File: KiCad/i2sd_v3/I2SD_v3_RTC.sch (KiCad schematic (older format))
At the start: 6 parts, among them U4 DS3231N

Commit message: i2sd_v3 : 2011 Nov 22 added INT/SQW 1Hz to PD2 port of ATMega via solder bridge, near Screw/RST Switch
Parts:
- added B20: I/O, I/O, symbol I/O
- added R9: 10k, symbol R
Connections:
- net labels added: 1Hz, B_03
- wire segments 35 -> 38
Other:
- note added: "Solder Bridge betn\nB2 & B20 to get 1Hz"
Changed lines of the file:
@@
-EESchema Schematic File Version 2  date 11/18/2011 6:47:08 PM
+EESchema Schematic File Version 2  date 11/22/2011 6:28:42 PM
 LIBS:i2sd_v3
 LIBS:power
@@
 Sheet 2 2
 Title "Buckler, i2sd, v3, with RTC, with HW addressing"
-Date "18 nov 2011"
+Date "22 nov 2011"
 Rev "3"
 Comp "WyoLum"
@@
 Comment4 ""
 $EndDescr
+Text Notes 7950 2225 2    50   ~ 0
+Solder Bridge betn\nB2 & B20 to get 1Hz
+Text HLabel 7825 2450 2    50   Input ~ 0
+B_03
+Text Label 7550 2450 0    50   ~ 0
+1Hz
+Wire Wire Line
+	7400 2450 7825 2450
+Connection ~ 6650 1675
+Wire Wire Line
+	6650 1850 6650 1675
+Wire Wire Line
+	7250 3750 7050 3750
+Wire Wire Line
+	7050 3750 7050 1675
+Wire Wire Line
+	7050 1675 4375 1675
+Wire Wire Line
+	6450 2600 6675 2600
+Wire Wire Line
+	7250 4000 4500 4000
+Wire Wire Line
+	4500 4000 4500 2850
+Wire Wire Line
+	4500 2850 4650 2850
+Connection ~ 3950 3100
+Wire Wire Line
+	3950 3100 4175 3100
+Wire Wire Line
+	4175 3100 4175 2975
+Wire Wire Line
+	3950 2550 3950 1900
+Wire Wire Line
+	3950 1900 5300 1900
+Connection ~ 6575 3150
+Wire Wire Line
+	6575 3150 6450 3150
+Connection ~ 6575 2950
+Wire Wire Line
+	6450 2950 6575 2950
+Connection ~ 5850 3750
+Wire Wire Line
+	5850 3750 5850 3650
+Wire Wire Line
+	5750 3750 5750 3650
+Wire Wire Line
+	6575 2850 6575 3750
+Wire Wire Line
+	6575 2850 6450 2850
+Wire Wire Line
+	4650 2600 4375 2600
+Connection ~ 5750 3750
+Wire Wire Line
+	5950 3750 5950 3650
+Connection ~ 5950 3750
+Wire Wire Line
+	6575 3050 6450 3050
+Connection ~ 6575 3050
+Wire Wire Line
+	6450 3250 6575 3250
+Connection ~ 6575 3250
+Wire Wire Line
+	4650 2450 4375 2450
+Wire Wire Line
+	3950 3000 3950 3750
+Wire Wire Line
+	3950 3750 6575 3750
+Connection ~ 4375 3750
+Wire Wire Line
+	4175 2575 4175 2425
+Wire Wire Line
+	4175 2425 3950 2425
+Connection ~ 3950 2425
+Wire Wire Line
+	4375 2450 4375 1675
+Wire Wire Line
+	4650 3000 4550 3000
+Wire Wire Line
+	4550 3000 4550 3875
+Wire Wire Line
+	4550 3875 7250 3875
+Wire Wire Line
+	6675 2450 6450 2450
+Wire Wire Line
+	6675 2750 6450 2750
+Wire Wire Line
+	4375 2600 4375 4125
+Wire Wire Line
+	4375 4125 7250 4125
+Wire Wire Line
+	5300 1850 5300 2000
+Connection ~ 5300 1900
+Wire Wire Line
+	6650 2350 6650 2450
+Connection ~ 6650 2450
+$Comp
+L I/O B20
+U 1 1 4ECB8D5B
+P 7250 2450
+F 0 "B20" H 7330 2450 40  0000 L CNN
+F 1 "I/O" H 7250 2505 30  0001 C CNN
+F 2 "I/O" H 7250 2450 60  0001 C CNN
+	1    7250 2450
+	-1   0    0    1
+$EndComp
+$Comp
+L R R9
+U 1 1 4ECB8D22
+P 6650 2100
+F 0 "R9" V 6730 2100 50  0000 C CNN
+F 1 "10k" V 6650 2100 50  0000 C CNN
+	1    6650 2100
+	1    0    0    -1
+$EndComp
 $Comp
 L +BATT #PWR09
@@
 	1    0    0    -1
 $EndComp
-Connection ~ 5300 1900
-Wire Wire Line
-	5300 1850 5300 2000
-Wire Wire Line
-	7250 4125 4375 4125
-Wire Wire Line
-	4375 4125 4375 2600
-Wire Wire Line
-	6675 2750 6450 2750
-Wire Wire Line
-	6675 2450 6450 2450
-Wire Wire Line
-	7250 3875 4550 3875
-Wire Wire Line
-	4550 3875 4550 3000
-Wire Wire Line
-	4550 3000 4650 3000
-Wire Wire Line
-	4375 2450 4375 1675
-Connection ~ 3950 2425
-Wire Wire Line
-	3950 2425 4175 2425
-Wire Wire Line
-	4175 2425 4175 2575
-Connection ~ 4375 3750
-Wire Wire Line
-	3950 3750 6575 3750
-Wire Wire Line
-	3950 3750 3950 3000
-Wire Wire Line
-	4375 2450 4650 2450
-Connection ~ 6575 3250
-Wire Wire Line
-	6450 3250 6575 3250
-Connection ~ 6575 3050
-Wire Wire Line
-	6575 3050 6450 3050
-Connection ~ 5950 3750
-Wire Wire Line
-	5950 3750 5950 3650
-Connection ~ 5750 3750
-Wire Wire Line
-	4375 2600 4650 2600
-Wire Wire Line
-	6450 2850 6575 2850
-Wire Wire Line
-	6575 2850 6575 3750
-Wire Wire Line
-	5750 3750 5750 3650
-Wire Wire Line
-	5850 3750 5850 3650
-Connection ~ 5850 3750
-Wire Wire Line
-	6450 2950 6575 2950
-Connection ~ 6575 2950
-Wire Wire Line
-	6575 3150 6450 3150
-Connection ~ 6575 3150
-Wire Wire Line
-	5300 1900 3950 1900
-Wire Wire Line
-	3950 1900 3950 2550
-Wire Wire Line
-	4175 2975 4175 3100
-Wire Wire Line
-	4175 3100 3950 3100
-Connection ~ 3950 3100
-Wire Wire Line
-	4650 2850 4500 2850
-Wire Wire Line
-	4500 2850 4500 4000
-Wire Wire Line
-	4500 4000 7250 4000
-Wire Wire Line
-	6450 2600 6675 2600
-Wire Wire Line
-	4375 1675 7050 1675
-Wire Wire Line
-	7050 1675 7050 3750
-Wire Wire Line
-	7050 3750 7250 3750
 Text HLabel 7250 4125 2    60   Input ~ 0
 GND

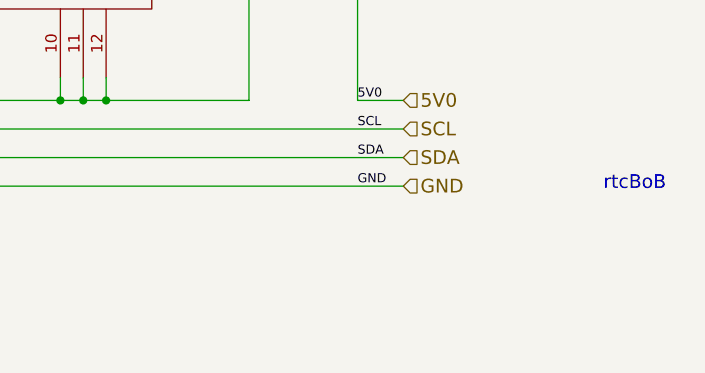
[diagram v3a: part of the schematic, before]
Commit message: i2sd_v3 : Silk screen changes, Box design, connected CD tracks
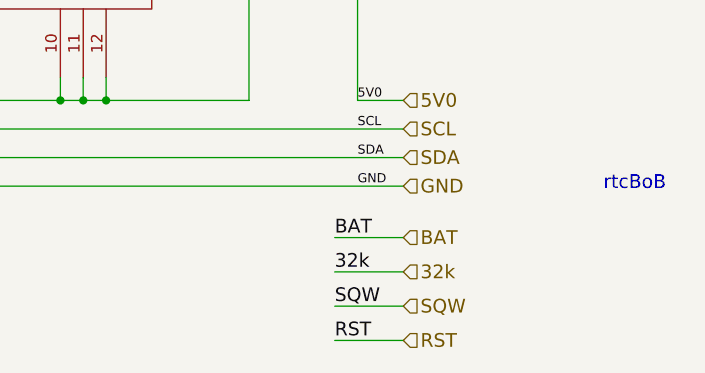
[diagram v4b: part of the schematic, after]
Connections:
- wire segments 38 -> 42
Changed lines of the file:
@@
-EESchema Schematic File Version 2  date 11/22/2011 6:28:42 PM
+EESchema Schematic File Version 2  date 1/12/2012 5:17:19 PM
 LIBS:i2sd_v3
 LIBS:power
@@
 Sheet 2 2
 Title "Buckler, i2sd, v3, with RTC, with HW addressing"
-Date "22 nov 2011"
+Date "12 jan 2012"
 Rev "3"
 Comp "WyoLum"
@@
 Comment4 ""
 $EndDescr
-Text Notes 7950 2225 2    50   ~ 0
-Solder Bridge betn\nB2 & B20 to get 1Hz
-Text HLabel 7825 2450 2    50   Input ~ 0
-B_03
-Text Label 7550 2450 0    50   ~ 0
-1Hz
+Text Label 6950 4800 0    60   ~ 0
+RST
+Text Label 6950 4650 0    60   ~ 0
+SQW
+Text Label 6950 4500 0    60   ~ 0
+32k
+Text Label 6950 4350 0    60   ~ 0
+BAT
+Wire Wire Line
+	7250 4800 6950 4800
+Wire Wire Line
+	7250 4500 6950 4500
 Wire Wire Line
 	7400 2450 7825 2450
@@
 	6650 2350 6650 2450
 Connection ~ 6650 2450
+Wire Wire Line
+	7250 4350 6950 4350
+Wire Wire Line
+	7250 4650 6950 4650
+Text HLabel 7250 4800 2    60   Input ~ 0
+RST
+Text HLabel 7250 4650 2    60   Input ~ 0
+SQW
+Text HLabel 7250 4500 2    60   Input ~ 0
+32k
+Text HLabel 7250 4350 2    60   Input ~ 0
+BAT
+Text Notes 7950 2225 2    50   ~ 0
+Solder Bridge betn\nB2 & B20 to get 1Hz
+Text HLabel 7825 2450 2    50   Input ~ 0
+B_03
+Text Label 7550 2450 0    50   ~ 0
+1Hz
 $Comp
 L I/O B20

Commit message: i2sd_v3 some minor pcb changes
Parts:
- removed B20: I/O, I/O, symbol I/O
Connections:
- net labels added: B_12
- net labels removed: B_03
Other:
- moved on the sheet: R9
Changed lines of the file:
@@
-EESchema Schematic File Version 2  date 1/12/2012 5:17:19 PM
+EESchema Schematic File Version 2  date 1/16/2012 6:29:58 PM
 LIBS:i2sd_v3
 LIBS:power
+LIBS:cmos4000
 LIBS:i2sd_v3-cache
 EELAYER 25  0
@@
 Sheet 2 2
 Title "Buckler, i2sd, v3, with RTC, with HW addressing"
-Date "12 jan 2012"
+Date "16 jan 2012"
 Rev "3"
 Comp "WyoLum"
@@
 Comment4 ""
 $EndDescr
+Connection ~ 6650 2350
+Wire Wire Line
+	6650 2350 7825 2350
+Wire Wire Line
+	7250 4650 6950 4650
+Wire Wire Line
+	7250 4350 6950 4350
+Connection ~ 6650 2450
+Wire Wire Line
+	6650 2250 6650 2450
+Connection ~ 5300 1900
+Wire Wire Line
+	5300 2000 5300 1850
+Wire Wire Line
+	7250 4125 4375 4125
+Wire Wire Line
+	4375 4125 4375 2600
+Wire Wire Line
+	6675 2750 6450 2750
+Wire Wire Line
+	6450 2450 6675 2450
+Wire Wire Line
+	7250 3875 4550 3875
+Wire Wire Line
+	4550 3875 4550 3000
+Wire Wire Line
+	4550 3000 4650 3000
+Wire Wire Line
+	4375 2450 4375 1675
+Connection ~ 3950 2425
+Wire Wire Line
+	3950 2425 4175 2425
+Wire Wire Line
+	4175 2425 4175 2575
+Connection ~ 4375 3750
+Wire Wire Line
+	3950 3750 6575 3750
+Wire Wire Line
+	3950 3750 3950 3000
+Wire Wire Line
+	4375 2450 4650 2450
+Connection ~ 6575 3250
+Wire Wire Line
+	6450 3250 6575 3250
+Connection ~ 6575 3050
+Wire Wire Line
+	6575 3050 6450 3050
+Connection ~ 5950 3750
+Wire Wire Line
+	5950 3750 5950 3650
+Connection ~ 5750 3750
+Wire Wire Line
+	4375 2600 4650 2600
+Wire Wire Line
+	6450 2850 6575 2850
+Wire Wire Line
+	6575 2850 6575 3750
+Wire Wire Line
+	5750 3750 5750 3650
+Wire Wire Line
+	5850 3750 5850 3650
+Connection ~ 5850 3750
+Wire Wire Line
+	6450 2950 6575 2950
+Connection ~ 6575 2950
+Wire Wire Line
+	6575 3150 6450 3150
+Connection ~ 6575 3150
+Wire Wire Line
+	5300 1900 3950 1900
+Wire Wire Line
+	3950 1900 3950 2550
+Wire Wire Line
+	4175 2975 4175 3100
+Wire Wire Line
+	4175 3100 3950 3100
+Connection ~ 3950 3100
+Wire Wire Line
+	4650 2850 4500 2850
+Wire Wire Line
+	4500 2850 4500 4000
+Wire Wire Line
+	4500 4000 7250 4000
+Wire Wire Line
+	6450 2600 6675 2600
+Wire Wire Line
+	4375 1675 7050 1675
+Wire Wire Line
+	7050 1675 7050 3750
+Wire Wire Line
+	7050 3750 7250 3750
+Wire Wire Line
+	6650 1750 6650 1675
+Connection ~ 6650 1675
+Wire Wire Line
+	7250 4500 6950 4500
+Wire Wire Line
+	7250 4800 6950 4800
 Text Label 6950 4800 0    60   ~ 0
 RST
@@
 Text Label 6950 4350 0    60   ~ 0
 BAT
-Wire Wire Line
-	7250 4800 6950 4800
-Wire Wire Line
-	7250 4500 6950 4500
-Wire Wire Line
-	7400 2450 7825 2450
-Connection ~ 6650 1675
-Wire Wire Line
-	6650 1850 6650 1675
-Wire Wire Line
-	7250 3750 7050 3750
-Wire Wire Line
-	7050 3750 7050 1675
-Wire Wire Line
-	7050 1675 4375 1675
-Wire Wire Line
-	6450 2600 6675 2600
-Wire Wire Line
-	7250 4000 4500 4000
-Wire Wire Line
-	4500 4000 4500 2850
-Wire Wire Line
-	4500 2850 4650 2850
-Connection ~ 3950 3100
-Wire Wire Line
-	3950 3100 4175 3100
-Wire Wire Line
-	4175 3100 4175 2975
-Wire Wire Line
-	3950 2550 3950 1900
-Wire Wire Line
-	3950 1900 5300 1900
-Connection ~ 6575 3150
-Wire Wire Line
-	6575 3150 6450 3150
-Connection ~ 6575 2950
-Wire Wire Line
-	6450 2950 6575 2950
-Connection ~ 5850 3750
-Wire Wire Line
-	5850 3750 5850 3650
-Wire Wire Line
-	5750 3750 5750 3650
-Wire Wire Line
-	6575 2850 6575 3750
-Wire Wire Line
-	6575 2850 6450 2850
-Wire Wire Line
-	4650 2600 4375 2600
-Connection ~ 5750 3750
-Wire Wire Line
-	5950 3750 5950 3650
-Connection ~ 5950 3750
-Wire Wire Line
-	6575 3050 6450 3050
-Connection ~ 6575 3050
-Wire Wire Line
-	6450 3250 6575 3250
-Connection ~ 6575 3250
-Wire Wire Line
-	4650 2450 4375 2450
-Wire Wire Line
-	3950 3000 3950 3750
-Wire Wire Line
-	3950 3750 6575 3750
-Connection ~ 4375 3750
-Wire Wire Line
-	4175 2575 4175 2425
-Wire Wire Line
-	4175 2425 3950 2425
-Connection ~ 3950 2425
-Wire Wire Line
-	4375 2450 4375 1675
-Wire Wire Line
-	4650 3000 4550 3000
-Wire Wire Line
-	4550 3000 4550 3875
-Wire Wire Line
-	4550 3875 7250 3875
-Wire Wire Line
-	6675 2450 6450 2450
-Wire Wire Line
-	6675 2750 6450 2750
-Wire Wire Line
-	4375 2600 4375 4125
-Wire Wire Line
-	4375 4125 7250 4125
-Wire Wire Line
-	5300 1850 5300 2000
-Connection ~ 5300 1900
-Wire Wire Line
-	6650 2350 6650 2450
-Connection ~ 6650 2450
-Wire Wire Line
-	7250 4350 6950 4350
-Wire Wire Line
-	7250 4650 6950 4650
 Text HLabel 7250 4800 2    60   Input ~ 0
 RST
@@
 Text HLabel 7250 4350 2    60   Input ~ 0
 BAT
-Text Notes 7950 2225 2    50   ~ 0
+Text Notes 7950 1950 2    50   ~ 0
 Solder Bridge betn\nB2 & B20 to get 1Hz
-Text HLabel 7825 2450 2    50   Input ~ 0
-B_03
-Text Label 7550 2450 0    50   ~ 0
+Text HLabel 7825 2350 2    50   Input ~ 0
+B_12
+Text Label 7550 2350 0    50   ~ 0
 1Hz
-$Comp
-L I/O B20
-U 1 1 4ECB8D5B
-P 7250 2450
-F 0 "B20" H 7330 2450 40  0000 L CNN
-F 1 "I/O" H 7250 2505 30  0001 C CNN
-F 2 "I/O" H 7250 2450 60  0001 C CNN
-	1    7250 2450
-	-1   0    0    1
-$EndComp
 $Comp
 L R R9
 U 1 1 4ECB8D22
-P 6650 2100
-F 0 "R9" V 6730 2100 50  0000 C CNN
-F 1 "10k" V 6650 2100 50  0000 C CNN
-	1    6650 2100
+P 6650 2000
+F 0 "R9" V 6730 2000 50  0000 C CNN
+F 1 "10k" V 6650 2000 50  0000 C CNN
+	1    6650 2000
 	1    0    0    -1
 $EndComp

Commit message: i2sd_v3 : BootDrive Header added, check it out, Justin
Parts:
- R9: footprint (none) -> r_0805
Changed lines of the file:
@@
-EESchema Schematic File Version 2  date 1/16/2012 6:29:58 PM
+EESchema Schematic File Version 2  date Sunday 19 February 2012 12:02:41 AM IST
 LIBS:i2sd_v3
 LIBS:power
-LIBS:cmos4000
 LIBS:i2sd_v3-cache
 EELAYER 25  0
@@
 Sheet 2 2
 Title "Buckler, i2sd, v3, with RTC, with HW addressing"
-Date "16 jan 2012"
+Date "18 feb 2012"
 Rev "3"
 Comp "WyoLum"
@@
 Comment4 ""
 $EndDescr
-Connection ~ 6650 2350
 Wire Wire Line
-	6650 2350 7825 2350
+	7250 4800 6950 4800
+Wire Wire Line
+	7250 4500 6950 4500
+Connection ~ 6650 1675
+Wire Wire Line
+	6650 1750 6650 1675
+Wire Wire Line
+	7250 3750 7050 3750
+Wire Wire Line
+	7050 1675 7050 3750
+Wire Wire Line
+	7050 1675 4375 1675
+Wire Wire Line
+	6450 2600 6675 2600
+Wire Wire Line
+	7250 4000 4500 4000
+Wire Wire Line
+	4500 4000 4500 2850
+Wire Wire Line
+	4500 2850 4650 2850
+Connection ~ 3950 3100
+Wire Wire Line
+	4175 3100 3950 3100
+Wire Wire Line
+	4175 3100 4175 2975
+Wire Wire Line
+	3950 2550 3950 1900
+Wire Wire Line
+	3950 1900 5300 1900
+Connection ~ 6575 3150
+Wire Wire Line
+	6575 3150 6450 3150
+Connection ~ 6575 2950
+Wire Wire Line
+	6450 2950 6575 2950
+Connection ~ 5850 3750
+Wire Wire Line
+	5850 3750 5850 3650
+Wire Wire Line
+	5750 3750 5750 3650
+Wire Wire Line
+	6575 3750 6575 2850
+Wire Wire Line
+	6575 2850 6450 2850
+Wire Wire Line
+	4375 2600 4650 2600
+Connection ~ 5750 3750
+Wire Wire Line
+	5950 3750 5950 3650
+Connection ~ 5950 3750
+Wire Wire Line
+	6575 3050 6450 3050
+Connection ~ 6575 3050
+Wire Wire Line
+	6450 3250 6575 3250
+Connection ~ 6575 3250
+Wire Wire Line
+	4650 2450 4375 2450
+Wire Wire Line
+	3950 3750 3950 3000
+Wire Wire Line
+	6575 3750 3950 3750
+Connection ~ 4375 3750
+Wire Wire Line
+	4175 2575 4175 2425
+Wire Wire Line
+	4175 2425 3950 2425
+Connection ~ 3950 2425
+Wire Wire Line
+	4375 2450 4375 1675
+Wire Wire Line
+	4650 3000 4550 3000
+Wire Wire Line
+	4550 3000 4550 3875
+Wire Wire Line
+	4550 3875 7250 3875
+Wire Wire Line
+	6450 2450 6675 2450
+Wire Wire Line
+	6675 2750 6450 2750
+Wire Wire Line
+	4375 4125 4375 2600
+Wire Wire Line
+	7250 4125 4375 4125
+Wire Wire Line
+	5300 2000 5300 1850
+Connection ~ 5300 1900
+Wire Wire Line
+	6650 2250 6650 2450
+Connection ~ 6650 2450
+Wire Wire Line
+	7250 4350 6950 4350
 Wire Wire Line
 	7250 4650 6950 4650
 Wire Wire Line
-	7250 4350 6950 4350
-Connection ~ 6650 2450
-Wire Wire Line
-	6650 2250 6650 2450
-Connection ~ 5300 1900
-Wire Wire Line
-	5300 2000 5300 1850
-Wire Wire Line
-	7250 4125 4375 4125
-Wire Wire Line
-	4375 4125 4375 2600
-Wire Wire Line
-	6675 2750 6450 2750
-Wire Wire Line
-	6450 2450 6675 2450
-Wire Wire Line
-	7250 3875 4550 3875
-Wire Wire Line
-	4550 3875 4550 3000
-Wire Wire Line
-	4550 3000 4650 3000
-Wire Wire Line
-	4375 2450 4375 1675
-Connection ~ 3950 2425
-Wire Wire Line
-	3950 2425 4175 2425
-Wire Wire Line
-	4175 2425 4175 2575
-Connection ~ 4375 3750
-Wire Wire Line
-	3950 3750 6575 3750
-Wire Wire Line
-	3950 3750 3950 3000
-Wire Wire Line
-	4375 2450 4650 2450
-Connection ~ 6575 3250
-Wire Wire Line
-	6450 3250 6575 3250
-Connection ~ 6575 3050
-Wire Wire Line
-	6575 3050 6450 3050
-Connection ~ 5950 3750
-Wire Wire Line
-	5950 3750 5950 3650
-Connection ~ 5750 3750
-Wire Wire Line
-	4375 2600 4650 2600
-Wire Wire Line
-	6450 2850 6575 2850
-Wire Wire Line
-	6575 2850 6575 3750
-Wire Wire Line
-	5750 3750 5750 3650
-Wire Wire Line
-	5850 3750 5850 3650
-Connection ~ 5850 3750
-Wire Wire Line
-	6450 2950 6575 2950
-Connection ~ 6575 2950
-Wire Wire Line
-	6575 3150 6450 3150
-Connection ~ 6575 3150
-Wire Wire Line
-	5300 1900 3950 1900
-Wire Wire Line
-	3950 1900 3950 2550
-Wire Wire Line
-	4175 2975 4175 3100
-Wire Wire Line
-	4175 3100 3950 3100
-Connection ~ 3950 3100
-Wire Wire Line
-	4650 2850 4500 2850
-Wire Wire Line
-	4500 2850 4500 4000
-Wire Wire Line
-	4500 4000 7250 4000
-Wire Wire Line
-	6450 2600 6675 2600
-Wire Wire Line
-	4375 1675 7050 1675
-Wire Wire Line
-	7050 1675 7050 3750
-Wire Wire Line
-	7050 3750 7250 3750
-Wire Wire Line
-	6650 1750 6650 1675
-Connection ~ 6650 1675
-Wire Wire Line
-	7250 4500 6950 4500
-Wire Wire Line
-	7250 4800 6950 4800
+	6650 2350 7825 2350
+Connection ~ 6650 2350
 Text Label 6950 4800 0    60   ~ 0
 RST
@@
 F 0 "R9" V 6730 2000 50  0000 C CNN
 F 1 "10k" V 6650 2000 50  0000 C CNN
+F 2 "r_0805" H 6650 2000 60  0001 C CNN
 	1    6650 2000
 	1    0    0    -1

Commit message: i2sd_v3 : legend clean up, DRC. PDF files added - SCH and PCB
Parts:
- BT1: footprint CR1632 -> CR2032
- C9: footprint c_0805 -> C2
- R9: footprint r_0805 -> rc03_vert_LED
- U4: footprint DS3231 -> DIP-24__600_ELL
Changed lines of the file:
@@
-EESchema Schematic File Version 2  date Sunday 19 February 2012 12:02:41 AM IST
+EESchema Schematic File Version 2  date 2/20/2012 3:18:38 PM
 LIBS:i2sd_v3
 LIBS:power
@@
 F 0 "R9" V 6730 2000 50  0000 C CNN
 F 1 "10k" V 6650 2000 50  0000 C CNN
-F 2 "r_0805" H 6650 2000 60  0001 C CNN
+F 2 "rc03_vert_LED" H 6650 2000 60  0001 C CNN
 	1    6650 2000
 	1    0    0    -1
@@
 F 0 "U4" H 5850 3350 60  0000 C CNN
 F 1 "DS3231N" H 5250 2400 60  0000 C CNN
-F 2 "DS3231" H 5550 2800 60  0001 C CNN
+F 2 "DIP-24__600_ELL" H 5550 2800 60  0001 C CNN
 	1    5550 2800
 	1    0    0    -1
@@
 F 0 "C9" V 4225 2875 50  0000 L CNN
 F 1 "100n" V 4225 2575 50  0000 L CNN
-F 2 "c_0805" H 4175 2775 60  0001 C CNN
+F 2 "C2" H 4175 2775 60  0001 C CNN
 	1    4175 2775
 	1    0    0    -1
@@
 F 0 "BT1" H 3650 2600 50  0000 C CNN
 F 1 "BATT_RTC" H 3950 2610 50  0000 C CNN
-F 2 "CR1632" H 3950 2800 60  0001 C CNN
+F 2 "CR2032" H 3950 2800 60  0001 C CNN
 F 4 "BU2032SM-HD-GCT-ND " H 3950 2800 60  0001 C CNN "Digikey"
 	1    3950 2800
